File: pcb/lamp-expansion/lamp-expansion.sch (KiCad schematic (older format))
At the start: 97 parts, among them IC1 PAM2421, IC10 74HC4050, IC2 MCP73811, IC3 AP2401, IC5 LM1117_3.3, IC6 LM1117_5.0, IC7 FT230X_SOP, IC8 TLV1117LV28, IC9 CC3000, J1 MICROUSB, J10 CC-IO, J2 DCIN, J3 SERIAL, J4 5PIN_INPUT, J5 2PIN_POWER, J6 2PIN_IO, J7 2PIN_POWER, J8 AVR_ISP, J9 UF.L, Q1 2N7002

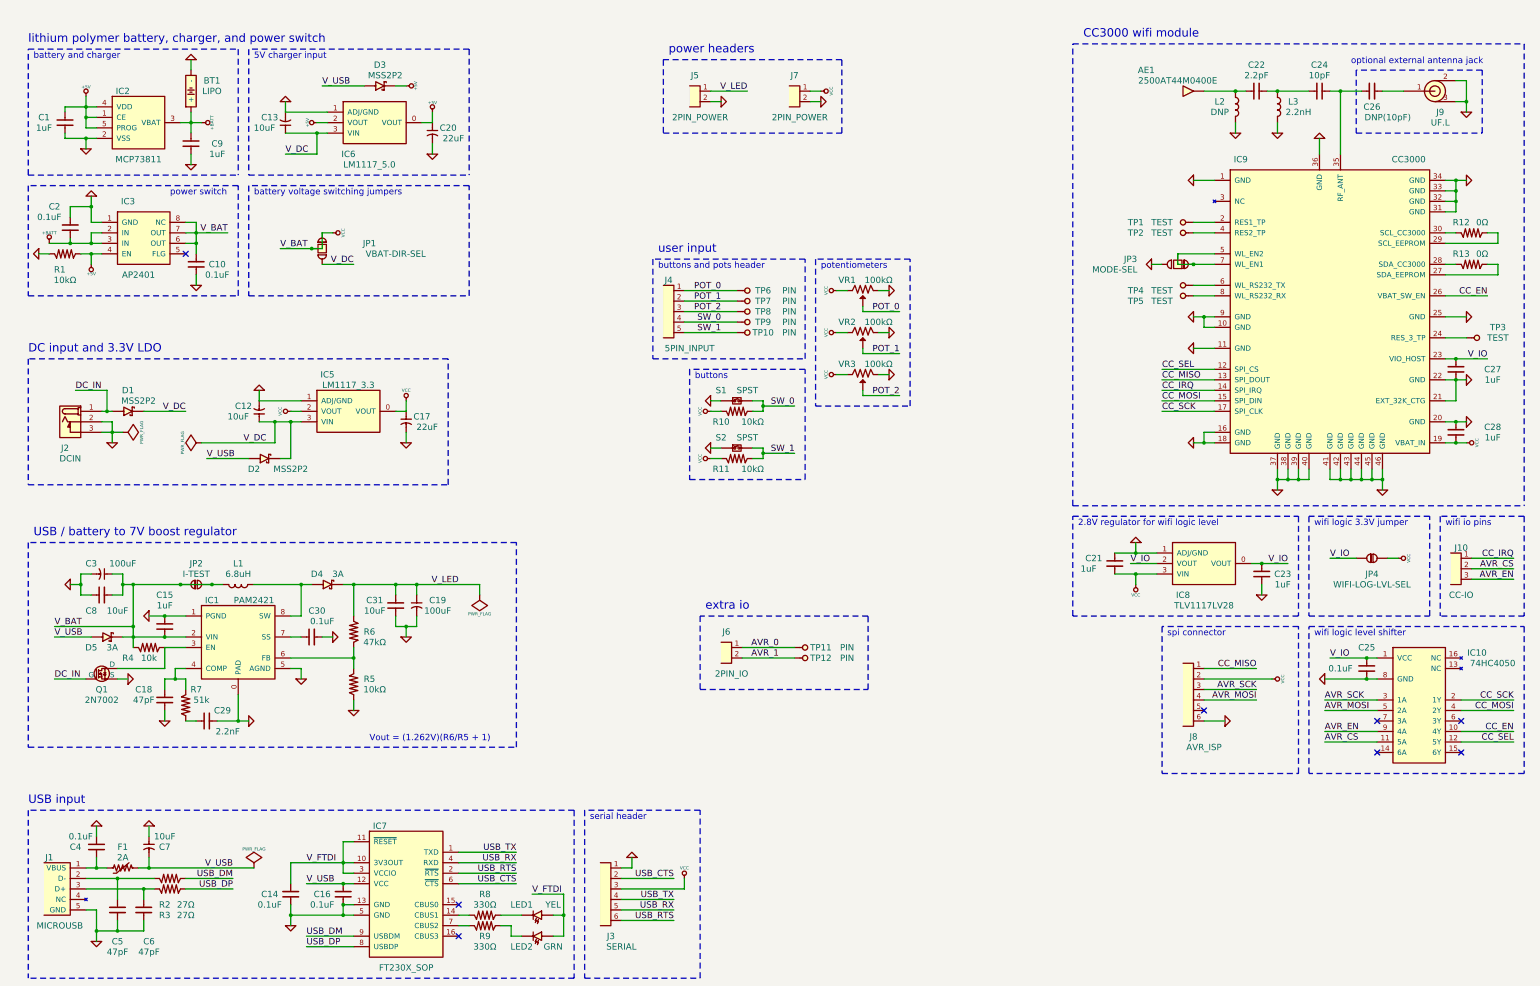
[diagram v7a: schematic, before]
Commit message: refactor power supply configuration
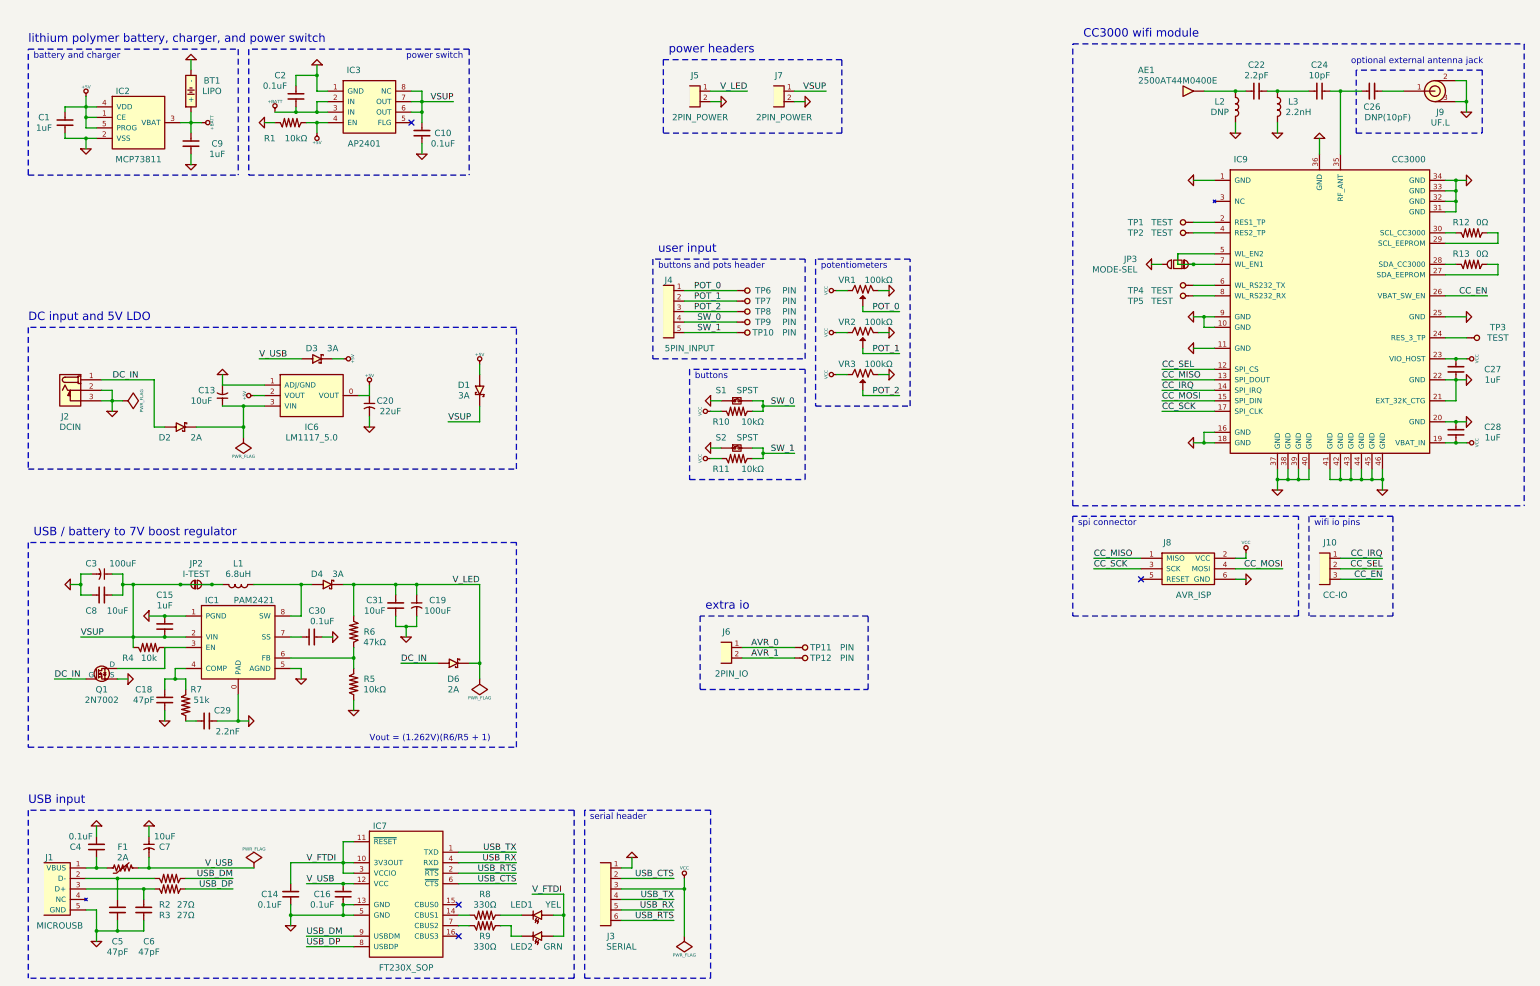
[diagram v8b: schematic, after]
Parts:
- removed C12: 10uF, symbol C_POL
- removed C17: 22uF, symbol C_POL
- removed C21, C23: 1uF, symbol C
- removed C25: 0.1uF, symbol C
- removed D5: 3A, symbol D_SCHOTTKY
- removed IC10: 74HC4050, symbol 74HC4050
- removed IC5: LM1117_3.3, symbol LM1117
- removed IC8: TLV1117LV28, symbol LM1117
- removed J8: AVR_ISP, symbol 6PIN_FEMALE
- removed JP1: VBAT-DIR-SEL, symbol JUMPER_3-PIN
- removed JP4: WIFI-LOG-LVL-SEL, symbol JUMPER_2-PIN
- added D6: 2A, symbol D_SCHOTTKY
- added J8: AVR_ISP, symbol AVR_ISP
- D1, D3: value MSS2P2 -> 3A; Distrib. Part MSS2P2-M3/89AGICT-ND -> RB056L-40TE25CT-ND; Manuf. Part MSS2P2-M3/89A -> RB056L-40TE25; Manufacturer Vishay -> Rohm Semiconductor
- D2: value MSS2P2 -> 2A
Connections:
- net AVR_CS is gone; now on net CC_SEL: J10.2
- net AVR_EN is gone; now on net CC_EN: J10.3
- net V_IO is gone; now on net VCC: C27.1, IC9.23 (VIO_HOST)
- net +5V: now also D1.2 (A)
- net CC_MISO: now also J8.1 (MISO)
- net CC_MOSI: now also J8.4 (MOSI)
- net CC_SCK: now also J8.3 (SCK)
- net DC_IN: now also D2.2 (A), D6.2 (A); no longer D1.2 (A)
- net GND: now also J8.6 (GND)
- net VCC: now also J8.2 (VCC); no longer C10.1, C15.2, C3.1, C8.1, IC1.2 (VIN), IC3.6 (OUT), IC3.7 (OUT), IC3.8 (NC), J7.1, JP2.1, JP2.2, L1.2, R4.1
- net V_LED: now also D6.1 (C)
- net V_USB: no longer D2.2 (A)
- net V_DC: no longer names the net of C13.1, D2.1 (C), IC6.3 (VIN)
- net V_DC: no longer D1.1 (C)
- new net VSUP: C10.1, C15.2, C3.1, C8.1, D1.1 (C), IC1.2 (VIN), IC3.6 (OUT), IC3.7 (OUT), IC3.8 (NC), J7.1, JP2.1, JP2.2, L1.2, R4.1
- no-connect marks 8 -> 4
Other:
- note added: "DC input and 5V LDO"
- note removed: "2.8V regulator for wifi logic level"
- note removed: "5V charger input"
- note removed: "DC input and 3.3V LDO"
- note removed: "battery voltage switching jumpers"
- note removed: "wifi logic 3.3V jumper"
- note removed: "wifi logic level shifter"
- moved on the sheet: C10, C13, C2, C20, D2, IC3, IC6, J10, J2, J7, R1
